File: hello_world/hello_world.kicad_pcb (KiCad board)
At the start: 2 copper layers, 99.1 x 76.2 mm, 15 parts, among them Q1 2N3904, U1 7555

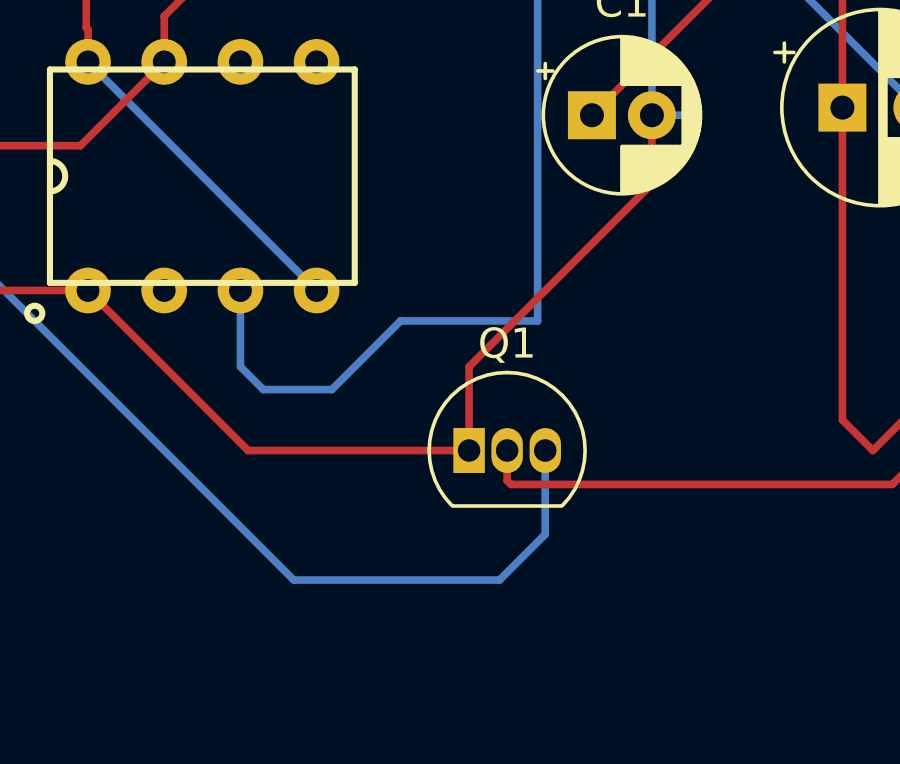
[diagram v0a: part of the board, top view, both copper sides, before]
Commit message: fixed TO-92 Inline for 2N3904 Transistor. Added additional 1mm spacing between pads. Adjusted footprint silkscreen and fab layers to make it bigger.
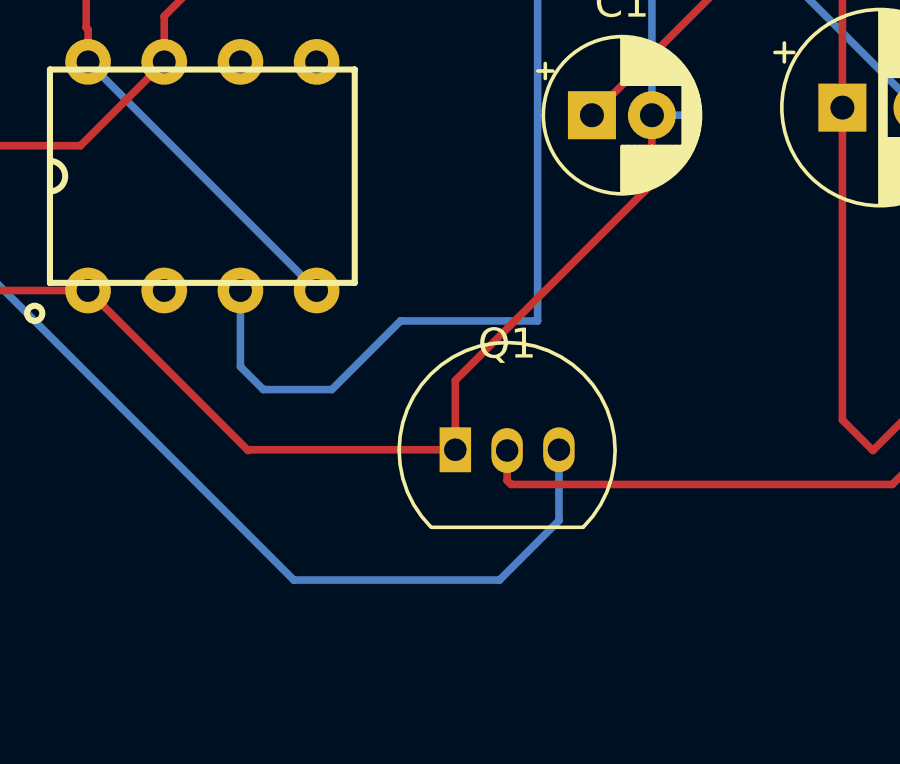
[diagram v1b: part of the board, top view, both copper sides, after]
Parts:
- Q1: footprint Package_TO_SOT_THT:TO-92_Inline -> hello_world:TO-92_Inline_fixed

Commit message: I guess this is a checkin
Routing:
- net GND: track 108.0 -> 109.9 mm
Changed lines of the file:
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@@
     (thickness 1.6)
     (drawings 9)
-    (tracks 91)
+    (tracks 94)
     (zones 0)
     (modules 15)
@@
   (segment (start 170.688 102.362) (end 174.498 106.172) (width 0.254) (layer B.Cu) (net 1))
   (segment (start 174.498 119.126) (end 176.022 119.126) (width 0.254) (layer B.Cu) (net 1))
-  (segment (start 174.498 110.022) (end 183.348 118.872) (width 0.254) (layer B.Cu) (net 1))
   (segment (start 174.498 106.68) (end 174.498 110.022) (width 0.254) (layer B.Cu) (net 1))
-  (segment (start 174.498 106.68) (end 174.498 119.126) (width 0.254) (layer B.Cu) (net 1))
   (segment (start 174.498 106.172) (end 174.498 106.68) (width 0.254) (layer B.Cu) (net 1))
   (segment (start 161.0614 130.2766) (end 167.9448 130.2766) (width 0.254) (layer F.Cu) (net 1))
@@
   (segment (start 174.498 119.126) (end 174.498 121.412) (width 0.254) (layer F.Cu) (net 1))
   (segment (start 174.498 121.412) (end 167.9448 127.9652) (width 0.254) (layer F.Cu) (net 1))
+  (segment (start 174.498 111.252) (end 179.832 111.252) (width 0.254) (layer B.Cu) (net 1))
+  (segment (start 174.498 111.252) (end 174.498 119.126) (width 0.254) (layer B.Cu) (net 1))
+  (segment (start 174.498 106.68) (end 174.498 111.252) (width 0.254) (layer B.Cu) (net 1))
+  (segment (start 183.348 114.768) (end 183.348 118.872) (width 0.254) (layer B.Cu) (net 1))
+  (segment (start 179.832 111.252) (end 183.348 114.768) (width 0.254) (layer B.Cu) (net 1))
   (segment (start 151.184999 105.181001) (end 150.225401 105.181001) (width 0.254) (layer F.Cu) (net 2))
   (segment (start 156.972 99.394) (end 151.184999 105.181001) (width 0.254) (layer F.Cu) (net 2))
